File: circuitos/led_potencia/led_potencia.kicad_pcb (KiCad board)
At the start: 2 copper layers, 234.7 x 180.9 mm, 268 parts, among them J1 Conn_01x02_Pin, J10 Conn_01x02_Pin, J11 Conn_01x02_Pin, J12 Conn_01x02_Pin, J13 Conn_01x02_Pin, J14 Conn_01x02_Pin, J15 Conn_01x02_Pin, J16 Conn_01x02_Pin, J17 Conn_01x02_Socket, J19 Conn_01x02_OE_GND, J2 Conn_01x02_Pin, J20 Conn_01x05_IN, J21 Conn_01x05_OUT, J3 Conn_01x02_Pin, J4 Conn_01x02_Pin, J5 Conn_01x02_Pin, J6 Conn_01x02_Pin, J7 Conn_01x02_Pin, J8 Conn_01x02_Pin, J9 Conn_01x02_Pin, Q1 IRLZ44N, Q18 IRF4905, Q19 IRF4905, Q2 IRLZ44N, Q20 IRF4905, Q21 PN2222A, Q22 PN2222A, Q23 PN2222A, Q24 IRF4905, Q25 PN2222A, Q3 IRLZ44N, Q4 IRLZ44N, U1 74HC595

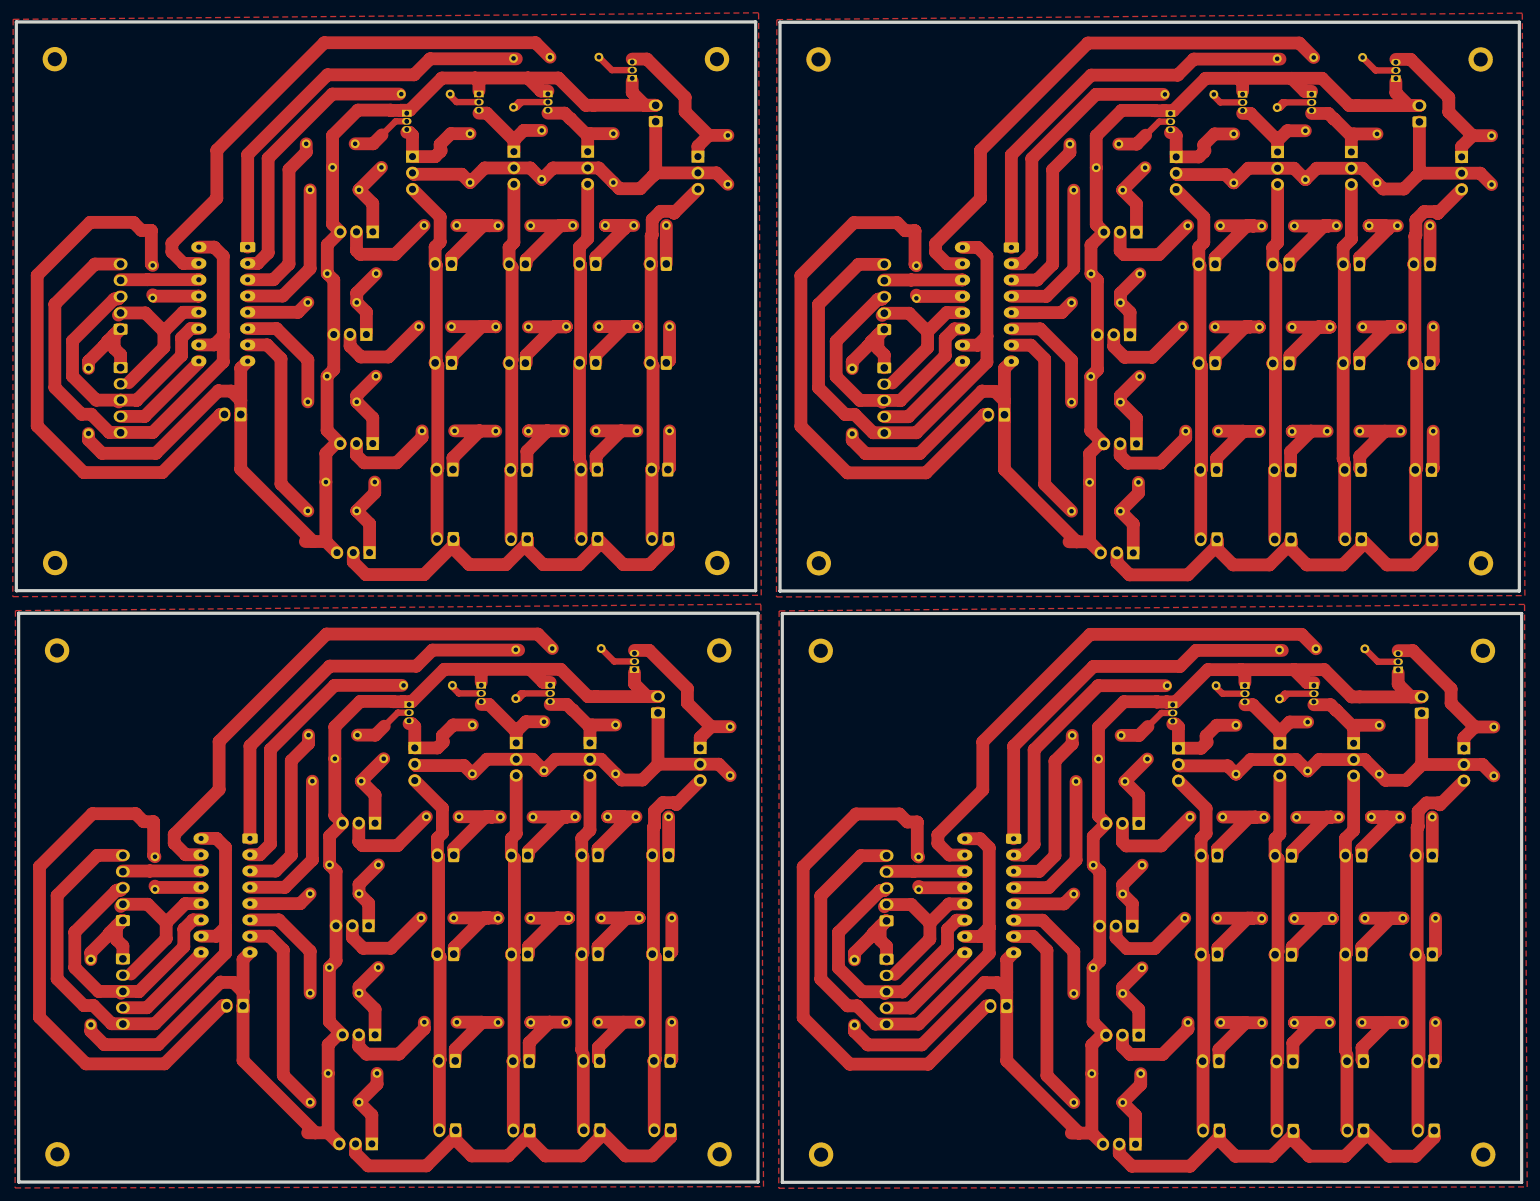
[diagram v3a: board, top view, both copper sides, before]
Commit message: script de testeo all on-off
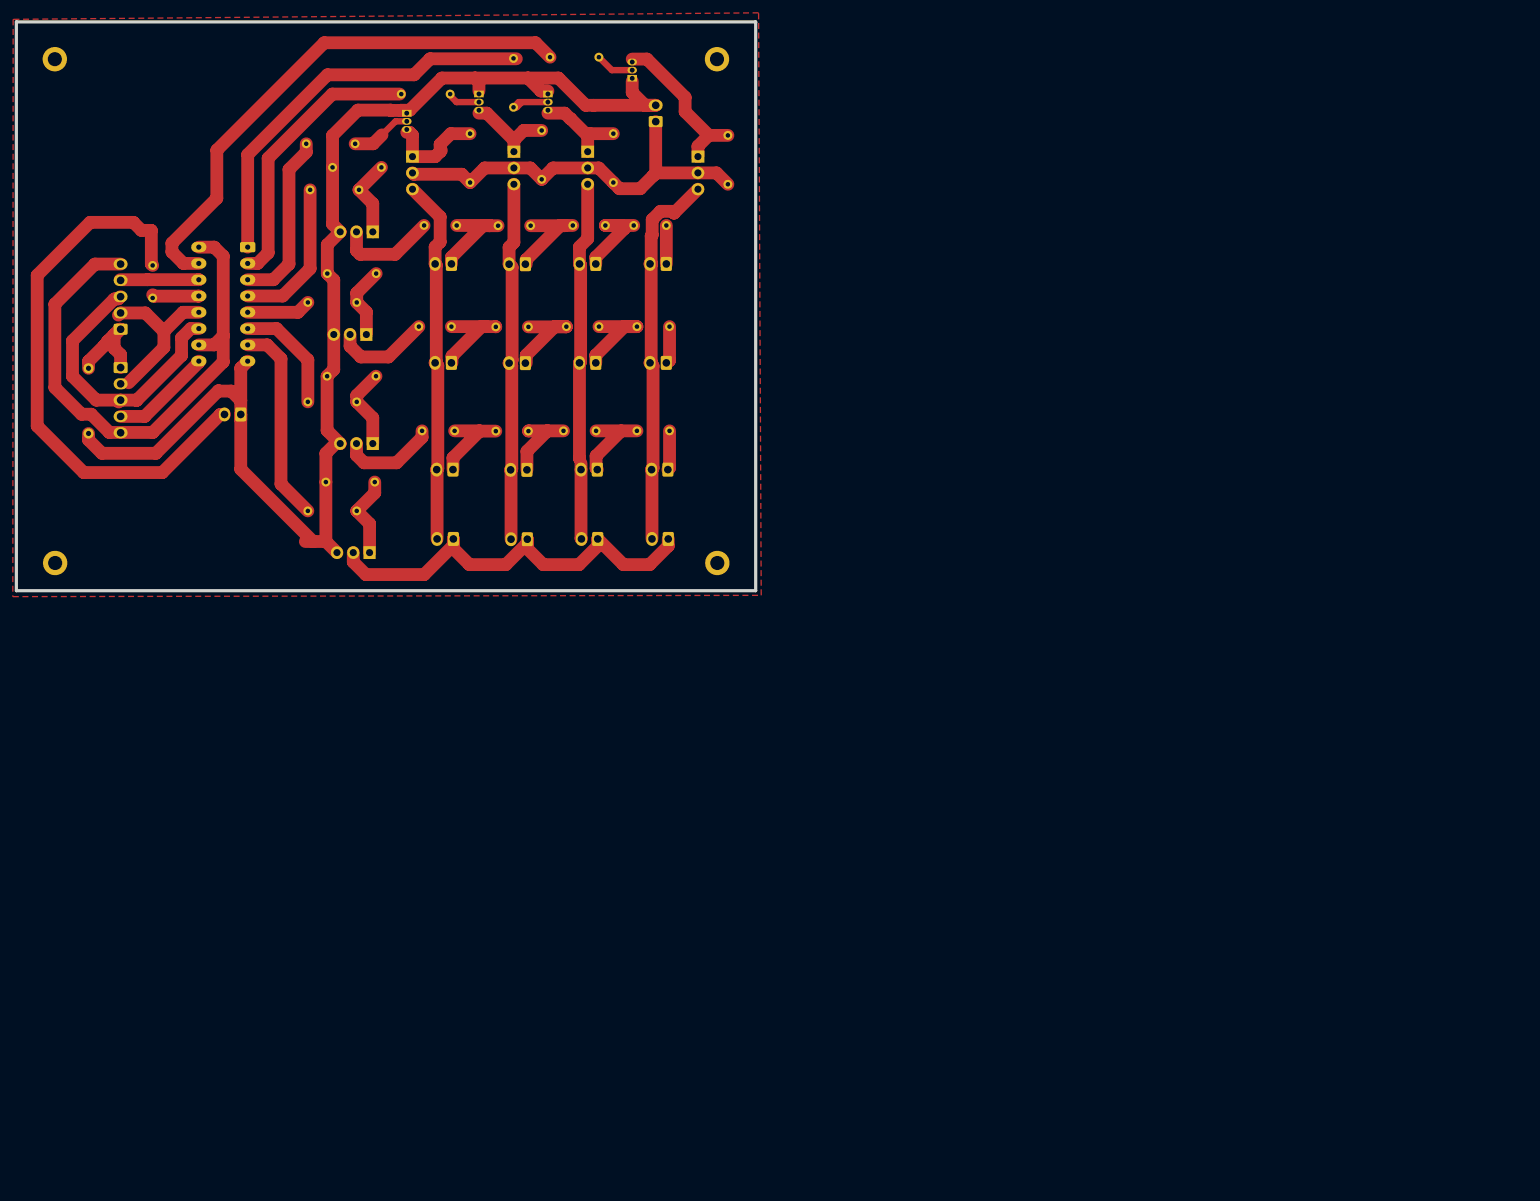
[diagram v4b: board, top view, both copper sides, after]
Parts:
- removed the H1 at (142.8, 98.9)
- removed the H1 at (143.2, 191.1)
- removed the H1 at (24.1, 191.1)
- removed the H2 at (246.1, 98.9)
- removed the H2 at (127.4, 191.1)
- removed the H2 at (246.4, 191.1)
- removed the H3 at (246.4, 112.6)
- removed the H3 at (246.0, 20.4)
- removed the H3 at (127.3, 112.5)
- removed the H4 at (24.1, 112.5)
- removed the H4 at (143.1, 112.6)
- removed the H4 at (142.8, 20.4)
- removed the J1 at (119.4, 144.5)
- removed the J1 at (238.5, 144.5)
- removed the J1 at (238.1, 52.3)
- removed the J10 at (227.7, 176.6)
- removed the J10 at (227.3, 84.4)
- removed the J10 at (108.7, 176.5)
- removed the J11 at (216.4, 84.4)
- removed the J11 at (97.7, 176.6)
- removed the J11 at (216.7, 176.6)
- removed the J12 at (86.2, 176.5)
- removed the J12 at (205.2, 176.6)
- removed the J12 at (204.8, 84.4)
- removed the J13 at (238.8, 187.4)
- removed the J13 at (238.4, 95.2)
- removed the J13 at (119.7, 187.3)
- removed the J14 at (108.7, 187.3)
- removed the J14 at (227.8, 187.4)
- removed the J14 at (227.4, 95.2)
- removed the J15 at (97.7, 187.4)
- removed the J15 at (216.8, 187.4)
- removed the J15 at (216.4, 95.2)
- removed the J16 at (205.3, 187.4)
- removed the J16 at (86.2, 187.3)
- removed the J16 at (204.9, 95.2)
- removed the J17 at (117.8, 122.3)
- removed the J17 at (236.4, 30.1)
- removed the J17 at (236.8, 122.3)
- removed the J19 at (172.1, 168.0)
- removed the J19 at (53.1, 167.9)
- removed the J19 at (171.8, 75.8)
- removed the J2 at (227.5, 144.5)
- removed the J2 at (108.4, 144.5)
- removed the J2 at (227.1, 52.3)
- removed the J20 at (153.4, 154.7)
- removed the J20 at (34.3, 154.6)
- removed the J20 at (153.0, 62.5)
- removed the J21 at (34.3, 160.6)
- removed the J21 at (153.0, 68.5)
- removed the J21 at (153.4, 160.7)
- removed the J3 at (216.1, 52.4)
- removed the J3 at (216.5, 144.5)
- removed the J3 at (97.4, 144.5)
- removed the J4 at (204.6, 52.3)
- removed the J4 at (85.9, 144.5)
- removed the J4 at (205.0, 144.5)
- removed the J5 at (238.5, 159.9)
- removed the J5 at (119.4, 159.9)
- removed the J5 at (238.1, 67.8)
- removed the J6 at (227.1, 67.8)
- removed the J6 at (108.4, 159.9)
- removed the J6 at (227.5, 159.9)
- removed the J7 at (97.4, 159.9)
- removed the J7 at (216.5, 160.0)
- removed the J7 at (216.1, 67.8)
- removed the J8 at (205.0, 159.9)
- removed the J8 at (204.6, 67.8)
- removed the J8 at (85.9, 159.9)
- removed the J9 at (119.7, 176.5)
- removed the J9 at (238.7, 176.6)
- removed the J9 at (238.3, 84.4)
- removed the Puente_GND1 at (148.4, 170.9)
- removed the Puente_GND1 at (29.3, 170.9)
- removed the Puente_GND1 at (148.0, 78.8)
- removed the Puente_OE1 at (39.3, 144.7)
- removed the Puente_OE1 at (158.0, 52.6)
- removed the Puente_OE1 at (158.4, 144.7)
- removed the Q1 at (191.8, 97.3)
- removed the Q1 at (73.2, 189.5)
- removed the Q1 at (192.2, 189.5)
- removed the Q18 at (124.3, 127.7)
- removed the Q18 at (243.0, 35.6)
- removed the Q18 at (243.4, 127.8)
- removed the Q19 at (107.2, 127.0)
- removed the Q19 at (226.2, 127.0)
- removed the Q19 at (225.8, 34.8)
- removed the Q2 at (192.7, 172.5)
- removed the Q2 at (192.3, 80.3)
- removed the Q2 at (73.7, 172.5)
- removed the Q20 at (214.3, 34.8)
- removed the Q20 at (95.7, 127.0)
- removed the Q20 at (214.7, 127.0)
- removed the Q21 at (114.1, 115.5)
- removed the Q21 at (232.8, 23.4)
- removed the Q21 at (233.1, 115.6)
- removed the Q22 at (101.0, 118.0)
- removed the Q22 at (220.0, 118.0)
- removed the Q22 at (219.6, 25.8)
- removed the Q23 at (209.2, 118.0)
- removed the Q23 at (90.2, 118.0)
- removed the Q23 at (208.9, 25.8)
- removed the Q24 at (198.9, 127.8)
- removed the Q24 at (79.8, 127.7)
- removed the Q24 at (198.5, 35.6)
- removed the Q25 at (197.6, 28.8)
- removed the Q25 at (198.0, 121.0)
- removed the Q25 at (79.0, 121.0)
- removed the Q3 at (72.7, 155.5)
- removed the Q3 at (191.3, 63.3)
- removed the Q3 at (191.7, 155.5)
- removed the Q4 at (192.7, 139.5)
- removed the Q4 at (73.7, 139.5)
- removed the Q4 at (192.3, 47.3)
- removed the R1 at (95.6, 112.4)
- removed the R1 at (214.6, 112.5)
- removed the R1 at (214.3, 20.3)
- removed the R11 at (248.1, 132.1)
- removed the R11 at (247.7, 39.9)
- removed the R11 at (129.0, 132.0)
- removed the R12 at (229.8, 39.6)
- removed the R12 at (111.2, 131.8)
- removed the R12 at (230.2, 131.8)
- removed the R13 at (219.0, 131.3)
- removed the R13 at (218.7, 39.1)
- removed the R13 at (100.0, 131.3)
- removed the R14 at (207.9, 131.8)
- removed the R14 at (207.5, 39.6)
- removed the R14 at (88.8, 131.8)
- removed the R17 at (75.0, 129.4)
- removed the R17 at (193.7, 37.3)
- removed the R17 at (194.1, 129.5)
- removed the R18 at (185.0, 86.3)
- removed the R18 at (66.3, 178.5)
- removed the R18 at (185.4, 178.5)
- removed the R19 at (66.6, 146.0)
- removed the R19 at (185.3, 53.8)
- removed the R19 at (185.6, 146.0)
- removed the R2 at (220.3, 112.3)
- removed the R2 at (101.3, 112.2)
- removed the R2 at (220.0, 20.1)
- removed the R20 at (74.2, 162.0)
- removed the R20 at (192.8, 69.8)
- removed the R20 at (193.2, 162.0)
- removed the R3 at (182.6, 183.0)
- removed the R3 at (63.5, 183.0)
- removed the R3 at (182.2, 90.8)
- removed the R4 at (63.9, 132.9)
- removed the R4 at (182.9, 133.0)
- removed the R4 at (182.6, 40.8)
- removed the R5 at (197.1, 118.0)
- removed the R5 at (78.1, 118.0)
- removed the R5 at (196.8, 25.9)
- removed the R6 at (182.3, 125.8)
- removed the R6 at (182.0, 33.6)
- removed the R6 at (63.3, 125.7)
- removed the R7 at (182.6, 166.0)
- removed the R7 at (182.2, 73.8)
- removed the R7 at (63.5, 166.0)
- removed the R8 at (182.2, 58.3)
- removed the R8 at (63.5, 150.5)
- removed the R8 at (182.6, 150.5)
- removed the U1 at (54.2, 141.8)
- removed the U1 at (172.8, 49.7)
- removed the U1 at (173.2, 141.9)
- removed the puente1 at (205.4, 46.3)
- removed the puente1 at (205.8, 138.5)
- removed the puente1 at (86.7, 138.5)
- removed the puente10 at (97.9, 170.5)
- removed the puente10 at (217.0, 170.6)
- removed the puente10 at (216.6, 78.4)
- removed the puente11 at (227.5, 170.5)
- removed the puente11 at (227.2, 78.4)
- removed the puente11 at (108.5, 170.5)
- removed the puente12 at (238.6, 78.4)
- removed the puente12 at (239.0, 170.5)
- removed the puente12 at (119.9, 170.5)
- removed the puente2 at (217.3, 138.5)
- removed the puente2 at (98.3, 138.5)
- removed the puente2 at (217.0, 46.4)
- removed the puente3 at (109.9, 138.5)
- removed the puente3 at (228.6, 46.3)
- removed the puente3 at (229.0, 138.5)
- removed the puente4 at (238.5, 138.5)
- removed the puente4 at (119.4, 138.5)
- removed the puente4 at (238.1, 46.3)
- removed the puente5 at (204.6, 62.1)
- removed the puente5 at (205.0, 154.3)
- removed the puente5 at (85.9, 154.2)
- removed the puente6 at (97.9, 154.3)
- removed the puente6 at (216.6, 62.1)
- removed the puente6 at (217.0, 154.3)
- removed the puente7 at (108.9, 154.2)
- removed the puente7 at (227.6, 62.1)
- removed the puente7 at (228.0, 154.3)
- removed the puente8 at (239.0, 154.3)
- removed the puente8 at (238.6, 62.1)
- removed the puente8 at (119.9, 154.2)
- removed the puente9 at (205.1, 78.4)
- removed the puente9 at (86.4, 170.5)
- removed the puente9 at (205.5, 170.5)
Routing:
- net GND: track 823.8 -> 206.0 mm
- net Net-(J19-Pin_2): track 346.8 -> 86.7 mm
- net VCC: track 339.3 -> 84.8 mm
- net Net-(U1-QA): track 334.0 -> 83.5 mm
- net Net-(J13-Pin_1): track 270.3 -> 67.6 mm
- net +12V: track 251.5 -> 62.9 mm
- net Net-(U1-QB): track 250.0 -> 62.5 mm
- net Net-(J1-Pin_2): track 238.9 -> 59.7 mm
- net Net-(J12-Pin_2): track 228.2 -> 57.1 mm
- net Net-(J11-Pin_2): track 225.2 -> 56.3 mm
- net Net-(J10-Pin_2): track 221.0 -> 55.2 mm
- net Net-(J20-Pin_3): track 175.1 -> 43.8 mm
- net Net-(U1-QC): track 173.1 -> 43.3 mm
- net Net-(U1-QH): track 126.2 -> 31.5 mm
- net Net-(U1-QD): track 109.3 -> 27.3 mm
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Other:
- board size 234.7 x 180.9 mm -> 115.2 x 88.7 mm

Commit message: nota para correccion
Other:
- board text added: "INVERTIR PISTAS DE VIN Y DE VCCGND YA QUE ESTAN EsPEJADAS"
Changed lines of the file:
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@@
 		)
 		(property "Value" "Conn_01x05_IN"
-			(at 5.08 -4.08 -90)
+			(at 5.08 -4.08 270)
 			(layer "F.Fab")
 			(effects
@@
 		)
 		(property "Value" "Conn_01x05_OUT"
-			(at 5.08 -4.08 -90)
+			(at 5.08 -4.08 270)
 			(layer "F.Fab")
 			(effects
@@
 		(layer "Edge.Cuts")
 	)
+	(gr_text "INVERTIR PISTAS DE VIN Y DE VCCGND YA QUE ESTAN EsPEJADAS"
+		(at 122.5296 30.607 0)
+		(layer "User.1")
+		(effects
+			(font
+				(size 1 1)
+				(thickness 0.15)
+			)
+			(justify left bottom)
+		)
+	)
 	(segment

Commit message: cambio irlz44n x8x2 subida pre simplificar
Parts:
- removed Puente_GND1: 0, Resistor_THT:R_Axial_DIN0207_L6.3mm_D2.5mm_P10.16mm_Horizontal
- removed Puente_OE1, puente1, puente10, puente11, puente12, puente2, puente3, puente4, puente5, puente6, puente7, puente8, puente9: 0, Resistor_THT:R_Axial_DIN0204_L3.6mm_D1.6mm_P5.08mm_Horizontal
- removed Q1, Q2, Q3, Q4: IRLZ44N, Package_TO_SOT_THT:TO-220-3_Vertical
- removed Q25: PN2222A, Package_TO_SOT_THT:TO-92_Inline
- removed R17, R18, R19, R20: 10k, Resistor_THT:R_Axial_DIN0204_L3.6mm_D1.6mm_P7.62mm_Horizontal
- added J18: Conn_01x02_Socket, Connector_Molex:Molex_KK-254_AE-6410-02A_1x02_P2.54mm_Vertical, F.Cu at (116.1, 160.6)
- added Q10: IRLZ44N, Package_TO_SOT_THT:TO-220-3_Vertical, F.Cu at (83.9, 77.4)
- added Q11: IRLZ44N, Package_TO_SOT_THT:TO-220-3_Vertical, F.Cu at (89.9, 77.4)
- added Q12: IRLZ44N, Package_TO_SOT_THT:TO-220-3_Vertical, F.Cu at (95.8, 77.4)
- added Q13: IRLZ44N, Package_TO_SOT_THT:TO-220-3_Vertical, F.Cu at (101.8, 77.4)
- added Q14: IRLZ44N, Package_TO_SOT_THT:TO-220-3_Vertical, F.Cu at (107.7, 77.4)
- added Q15: IRLZ44N, Package_TO_SOT_THT:TO-220-3_Vertical, F.Cu at (114.2, 77.1)
- added Q16: IRLZ44N, Package_TO_SOT_THT:TO-220-3_Vertical, F.Cu at (127.2, 72.5)
- added Q17: IRLZ44N, Package_TO_SOT_THT:TO-220-3_Vertical, F.Cu at (161.3, 81.3)
- added Q9: IRLZ44N, Package_TO_SOT_THT:TO-220-3_Vertical, F.Cu at (64.1, 78.0)
- added R10: 1k, Resistor_THT:R_Axial_DIN0204_L3.6mm_D1.6mm_P7.62mm_Horizontal, F.Cu at (195.8, 138.0)
- added R15: 1k, Resistor_THT:R_Axial_DIN0204_L3.6mm_D1.6mm_P7.62mm_Horizontal, F.Cu at (188.9, 39.5)
- added R16: 1k, Resistor_THT:R_Axial_DIN0204_L3.6mm_D1.6mm_P7.62mm_Horizontal, F.Cu at (155.7, 93.6)
- added R25: 10k, Resistor_THT:R_Axial_DIN0204_L3.6mm_D1.6mm_P7.62mm_Horizontal, F.Cu at (56.7, 79.6)
- added R26: 10k, Resistor_THT:R_Axial_DIN0204_L3.6mm_D1.6mm_P7.62mm_Horizontal, F.Cu at (94.0, 57.7)
- added R27: 10k, Resistor_THT:R_Axial_DIN0204_L3.6mm_D1.6mm_P7.62mm_Horizontal, F.Cu at (97.5, 64.7)
- added R28: 10k, Resistor_THT:R_Axial_DIN0204_L3.6mm_D1.6mm_P7.62mm_Horizontal, F.Cu at (100.3, 57.1)
- added R29: 10k, Resistor_THT:R_Axial_DIN0204_L3.6mm_D1.6mm_P7.62mm_Horizontal, F.Cu at (103.3, 65.5)
- added R30: 10k, Resistor_THT:R_Axial_DIN0204_L3.6mm_D1.6mm_P7.62mm_Horizontal, F.Cu at (106.3, 58.1)
- added R31: 10k, Resistor_THT:R_Axial_DIN0204_L3.6mm_D1.6mm_P7.62mm_Horizontal, F.Cu at (110.4, 65.6)
- added R32: 10k, Resistor_THT:R_Axial_DIN0204_L3.6mm_D1.6mm_P7.62mm_Horizontal, F.Cu at (121.7, 65.9)
- added R33: 10k, Resistor_THT:R_Axial_DIN0204_L3.6mm_D1.6mm_P7.62mm_Horizontal, F.Cu at (153.6, 81.6)
- added R34: 10k, Resistor_THT:R_Axial_DIN0204_L3.6mm_D1.6mm_P7.62mm_Horizontal, F.Cu at (192.1, 23.7)
- added R35: 10k, Resistor_THT:R_Axial_DIN0204_L3.6mm_D1.6mm_P7.62mm_Horizontal, F.Cu at (193.9, 48.2)
- added R36: 10k, Resistor_THT:R_Axial_DIN0204_L3.6mm_D1.6mm_P7.62mm_Horizontal, F.Cu at (196.3, 60.3)
- added R37: 10k, Resistor_THT:R_Axial_DIN0204_L3.6mm_D1.6mm_P7.62mm_Horizontal, F.Cu at (202.1, 86.1)
- added R38: 10k, Resistor_THT:R_Axial_DIN0204_L3.6mm_D1.6mm_P7.62mm_Horizontal, F.Cu at (196.3, 101.8)
- added R39: 10k, Resistor_THT:R_Axial_DIN0204_L3.6mm_D1.6mm_P7.62mm_Horizontal, F.Cu at (202.6, 129.8)
- added R40: 10k, Resistor_THT:R_Axial_DIN0204_L3.6mm_D1.6mm_P7.62mm_Horizontal, F.Cu at (200.4, 143.4)
- added R9: 1k, Resistor_THT:R_Axial_DIN0204_L3.6mm_D1.6mm_P7.62mm_Horizontal, F.Cu at (191.5, 156.6)
- added U2: 74HC595, Package_DIP:DIP-16_W7.62mm_Socket_LongPads, F.Cu at (172.5, 121.9)
- H1, H2, H3, H4, J1, J10, J11, J12, J13, J14, J15, J16, J17, J2, J20, J21, J3, J4, J5, J6, J7, J8, J9, R1, R2, R3, R4, R5, R6, R7, R8, U1: moved to F.Cu
- J19: value Conn_01x02_OE_GND -> Conn_01x02_Socket; moved to F.Cu
- Q18, Q19, Q20, Q24: value IRF4905 -> IRLZ44N; moved to F.Cu
- Q21, Q22, Q23: value PN2222A -> IRLZ44N; footprint Package_TO_SOT_THT:TO-92_Inline -> Package_TO_SOT_THT:TO-220-3_Vertical; moved to F.Cu
- R11, R12, R13, R14: value 10k -> 1k; moved to F.Cu
- moved H4 255.6 mm to (256.9, 124.9)
- moved H1 234.4 mm to (258.0, 106.3)
- moved Q24 172.0 mm to (207.3, 150.6), turned to 90 degrees
- moved H3 163.5 mm to (256.9, 119.6)
- moved Q23 157.0 mm to (208.1, 129.1), turned to 90 degrees
- moved J16 138.8 mm to (215.7, 144.1), turned to -90 degrees
- moved Q22 131.4 mm to (202.5, 108.7), turned to 90 degrees
- moved H2 130.8 mm to (256.9, 114.2)
- moved J12 127.2 mm to (211.0, 61.9), turned to -90 degrees
- moved J15 120.4 mm to (214.3, 124.0), turned to -90 degrees
- moved J11 119.4 mm to (209.0, 42.1), turned to -90 degrees
- moved J10 115.8 mm to (207.9, 25.3), turned to -90 degrees
- moved Q21 113.5 mm to (208.7, 85.5)
- moved Q20 113.4 mm to (203.6, 68.4), turned to 90 degrees
- moved R11 104.9 mm to (196.2, 120.2)
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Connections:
- J1 pad 1: Net-(J1-Pin_1) -> +12V
- J10 pad 1: Net-(J10-Pin_1) -> +12V
- J11 pad 1: Net-(J11-Pin_1) -> +12V
- J12 pad 1: Net-(J12-Pin_1) -> +12V
- J13 pad 1: Net-(J13-Pin_1) -> +12V
- J13 pad 2: Net-(J1-Pin_2) -> Net-(J13-Pin_2)
- J14 pad 1: Net-(J13-Pin_1) -> +12V
- J14 pad 2: Net-(J10-Pin_2) -> Net-(J14-Pin_2)
- J15 pad 1: Net-(J13-Pin_1) -> +12V
- J15 pad 2: Net-(J11-Pin_2) -> Net-(J15-Pin_2)
- J16 pad 1: Net-(J13-Pin_1) -> +12V
- J16 pad 2: Net-(J12-Pin_2) -> Net-(J16-Pin_2)
- J19 pad 1: GND -> VCC
- J2 pad 1: Net-(J2-Pin_1) -> +12V
- J2 pad 2: Net-(J10-Pin_2) -> Net-(J2-Pin_2)
- J20 pad 1: Net-(J20-Pin_1) -> Net-(J19-Pin_2)
- J21 pad 1: Net-(J20-Pin_1) -> Net-(J19-Pin_2)
- J3 pad 1: Net-(J3-Pin_1) -> +12V
- J3 pad 2: Net-(J11-Pin_2) -> Net-(J3-Pin_2)
- J4 pad 1: Net-(J4-Pin_1) -> +12V
- J4 pad 2: Net-(J12-Pin_2) -> Net-(J4-Pin_2)
- J5 pad 1: Net-(J5-Pin_1) -> +12V
- J5 pad 2: Net-(J1-Pin_2) -> Net-(J5-Pin_2)
- J6 pad 1: Net-(J6-Pin_1) -> +12V
- J6 pad 2: Net-(J10-Pin_2) -> Net-(J6-Pin_2)
- J7 pad 1: Net-(J7-Pin_1) -> +12V
- J7 pad 2: Net-(J11-Pin_2) -> Net-(J7-Pin_2)
- J8 pad 1: Net-(J8-Pin_1) -> +12V
- J8 pad 2: Net-(J12-Pin_2) -> Net-(J8-Pin_2)
- J9 pad 1: Net-(J9-Pin_1) -> +12V
- J9 pad 2: Net-(J1-Pin_2) -> Net-(J9-Pin_2)
- Q18 pad 2: +12V -> Net-(J10-Pin_2)
- Q18 pad 3: Net-(J1-Pin_2) -> GND
- Q19 pad 2: +12V -> Net-(J11-Pin_2)
- Q19 pad 3: Net-(J10-Pin_2) -> GND
- Q20 pad 2: +12V -> Net-(J12-Pin_2)
- Q20 pad 3: Net-(J11-Pin_2) -> GND
- Q21 pad 1: GND -> Net-(Q21-G)
- Q21 pad 2: Net-(Q21-B) -> Net-(J13-Pin_2)
- Q21 pad 3: Net-(Q18-G) -> GND
- Q22 pad 1: GND -> Net-(Q22-G)
- Q22 pad 2: Net-(Q22-B) -> Net-(J14-Pin_2)
- Q22 pad 3: Net-(Q19-G) -> GND
- Q23 pad 1: GND -> Net-(Q23-G)
- Q23 pad 2: Net-(Q23-B) -> Net-(J15-Pin_2)
- Q23 pad 3: Net-(Q20-G) -> GND
- Q24 pad 2: +12V -> Net-(J16-Pin_2)
- Q24 pad 3: Net-(J12-Pin_2) -> GND
- R1 pad 2: Net-(Q22-B) -> Net-(Q15-G)
- R11 pad 1: +12V -> Net-(U2-QC)
- R11 pad 2: Net-(Q18-G) -> Net-(Q22-G)
- R12 pad 1: +12V -> Net-(U2-QD)
- R12 pad 2: Net-(Q19-G) -> Net-(Q21-G)
- R13 pad 1: +12V -> Net-(U2-QE)
- R14 pad 1: +12V -> Net-(U2-QF)
- R14 pad 2: Net-(Q24-G) -> Net-(Q19-G)
- R2 pad 2: Net-(Q21-B) -> Net-(Q16-G)
- R5 pad 2: Net-(Q23-B) -> Net-(Q14-G)
- U1 pad 11: Net-(J20-Pin_3) -> Net-(J20-Pin_2)
- U1 pad 12: Net-(J20-Pin_2) -> Net-(J20-Pin_3)
- U1 pad 13: Net-(U1-~{OE}) -> Net-(Q10-S)
- U1 pad 8: GND -> Net-(Q10-S)
- U1 pad 9: Net-(J21-Pin_4) -> Net-(U1-QH')
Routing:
- net GND: track 206.0 -> 0.00 mm
- net Net-(J19-Pin_2): track 86.7 -> 0.00 mm
- net VCC: track 84.8 -> 0.00 mm
- net Net-(U1-QA): track 83.5 -> 0.00 mm
- net Net-(J13-Pin_1): track 67.6 -> 0.00 mm
- net +12V: track 62.9 -> 0.00 mm
- net Net-(U1-QB): track 62.5 -> 0.00 mm
- net Net-(J1-Pin_2): track 59.7 -> 0.00 mm
- net Net-(J12-Pin_2): track 57.1 -> 0.00 mm
- net Net-(J11-Pin_2): track 56.3 -> 0.00 mm
- net Net-(J10-Pin_2): track 55.2 -> 0.00 mm
- net Net-(J20-Pin_3): track 43.8 -> 0.00 mm
- net Net-(U1-QC): track 43.3 -> 0.00 mm
- net Net-(U1-QH): track 31.5 -> 0.00 mm
- net Net-(U1-QD): track 27.3 -> 0.00 mm
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- removed copper zone on F.Cu, net GND
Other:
- board outline removed
- board text removed: "INVERTIR PISTAS DE VIN Y DE VCCGND YA QUE ESTAN EsPEJADAS"

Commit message: simplificacion juegos de 1 ic x pcb 8 irlzn
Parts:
- removed J1, J2, J3, J4, J5, J6, J7, J8: Conn_01x02_Pin, Connector_Molex:Molex_KK-254_AE-6410-02A_1x02_P2.54mm_Vertical
- removed Q10, Q11, Q12, Q13, Q14, Q15, Q16, Q9: IRLZ44N, Package_TO_SOT_THT:TO-220-3_Vertical
- removed R1, R2, R3, R4, R5, R6, R7, R8: 1k, Resistor_THT:R_Axial_DIN0204_L3.6mm_D1.6mm_P7.62mm_Horizontal
- removed R25, R26, R27, R28, R29, R30, R31, R32: 10k, Resistor_THT:R_Axial_DIN0204_L3.6mm_D1.6mm_P7.62mm_Horizontal
- removed the U1 at (123.1, 102.1)
- moved J17 54.1 mm to (119.9, 69.8)
- moved J18 41.0 mm to (156.9, 157.6), turned to 90 degrees
- moved J20 37.5 mm to (147.2, 112.5), turned to -90 degrees
- moved J21 28.0 mm to (124.9, 112.5), turned to -90 degrees
- moved J19 14.7 mm to (88.7, 122.0), turned to 90 degrees
- renumbered U2 to U1
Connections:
- U1 pad 14: Net-(U1-QH') -> Net-(J20-Pin_4)
